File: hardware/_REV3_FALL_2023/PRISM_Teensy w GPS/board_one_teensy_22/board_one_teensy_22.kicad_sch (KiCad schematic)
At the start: 24 parts, among them J1 Micro_SD_Card_Det_Hirose_DM3AT, J3 3387, U1 Teensy4.0, U2 GPS-14414, U3 3966, U4 RFM69HCW_Breakout, U5 SFN-1407PA7.6

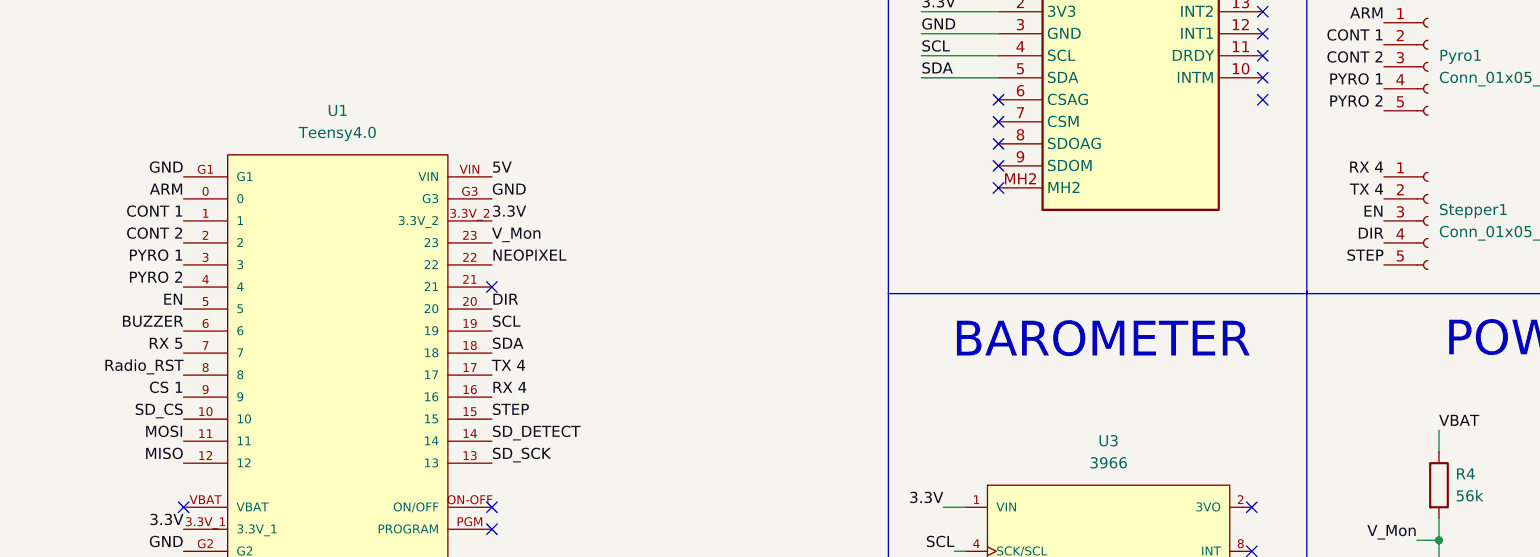
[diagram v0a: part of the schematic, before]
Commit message: fixed stepper wiring
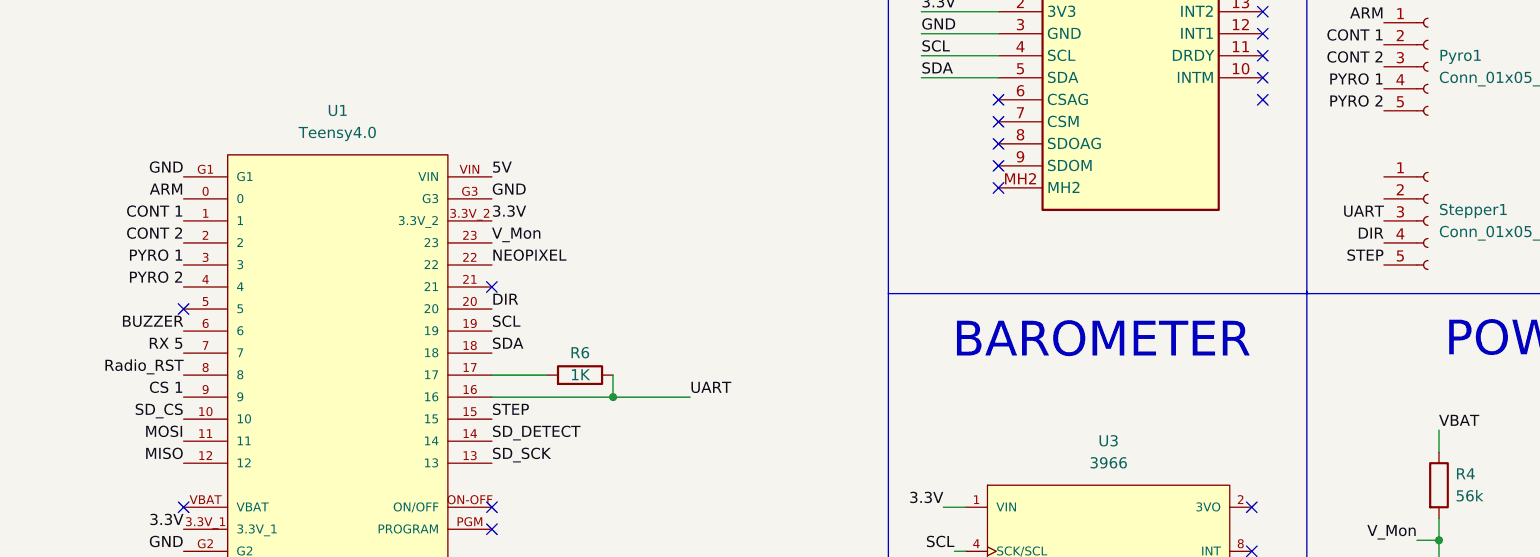
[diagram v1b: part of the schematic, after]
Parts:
- added R6: 1K, Resistor_SMD:R_0603_1608Metric, symbol Device:R
- D3, D5: Vendor (none) -> C2761795
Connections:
- net EN: no longer names the net of U1.5
- net EN: no longer Stepper1.3 (Pin_3)
- net RX 4: no longer names the net of Stepper1.1 (Pin_1)
- net RX 4: no longer U1.16
- net TX 4: no longer names the net of U1.17
- net TX 4: now also R6.2; no longer Stepper1.2 (Pin_2)
- new net UART: R6.1, Stepper1.3 (Pin_3), U1.16
- no-connect marks 35 -> 36
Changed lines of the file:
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@@
   (junction (at 248.92 27.94) (diameter 0) (color 0 0 0 0)
+  )
+  (junction (at 93.98 82.55) (diameter 0) (color 0 0 0 0)
   )
   (junction (at 55.88 177.8) (diameter 0) (color 0 0 0 0)
@@
   (no_connect (at 261.62 97.79))
   (no_connect (at 138.43 35.56))
+  (no_connect (at 44.45 72.39))
   (no_connect (at 261.62 102.87))
   (no_connect (at 138.43 50.8))
@@
     (stroke (width 0) (type default))
   )
+  (wire (pts (xy 93.98 82.55) (xy 102.87 82.55))
+    (stroke (width 0) (type default))
+  )
   (wire (pts (xy 231.14 27.94) (xy 231.14 34.29))
     (stroke (width 0) (type default))
@@
     (stroke (width 0) (type default))
   )
+  (wire (pts (xy 80.01 82.55) (xy 93.98 82.55))
+    (stroke (width 0) (type default))
+  )
   (wire (pts (xy 129.54 45.72) (xy 138.43 45.72))
     (stroke (width 0) (type default))
@@
     (stroke (width 0) (type default))
   )
+  (wire (pts (xy 93.98 80.01) (xy 93.98 82.55))
+    (stroke (width 0) (type default))
+  )
   (wire (pts (xy 40.64 171.45) (xy 34.925 171.45))
     (stroke (width 0) (type default))
@@
   )
   (polyline (pts (xy 125.73 128.905) (xy 173.99 128.905))
+    (stroke (width 0) (type default))
+  )
+  (wire (pts (xy 80.01 80.01) (xy 86.36 80.01))
     (stroke (width 0) (type default))
   )
@@
     (effects (font (size 1.27 1.27)) (justify left bottom))
   )
-  (label "EN" (at 44.45 72.39 180) (fields_autoplaced)
-    (effects (font (size 1.27 1.27)) (justify right bottom))
-  )
   (label "ARM" (at 44.45 59.69 180) (fields_autoplaced)
     (effects (font (size 1.27 1.27)) (justify right bottom))
@@
     (effects (font (size 1.27 1.27)) (justify right bottom))
   )
+  (label "UART" (at 182.88 62.23 180) (fields_autoplaced)
+    (effects (font (size 1.27 1.27)) (justify right bottom))
+  )
   (label "SD_SCK" (at 135.255 171.45 0) (fields_autoplaced)
     (effects (font (size 1.27 1.27)) (justify left bottom))
@@
     (effects (font (size 1.27 1.27)) (justify right bottom))
   )
-  (label "TX 4" (at 182.88 59.69 180) (fields_autoplaced)
-    (effects (font (size 1.27 1.27)) (justify right bottom))
-  )
   (label "SCL" (at 246.38 105.41 180) (fields_autoplaced)
     (effects (font (size 1.27 1.27)) (justify right bottom))
@@
     (effects (font (size 1.27 1.27)) (justify right bottom))
   )
-  (label "RX 4" (at 80.01 82.55 0) (fields_autoplaced)
-    (effects (font (size 1.27 1.27)) (justify left bottom))
-  )
   (label "CONT 2" (at 44.45 64.77 180) (fields_autoplaced)
     (effects (font (size 1.27 1.27)) (justify right bottom))
@@
     (effects (font (size 1.27 1.27)) (justify left bottom))
   )
-  (label "TX 4" (at 80.01 80.01 0) (fields_autoplaced)
-    (effects (font (size 1.27 1.27)) (justify left bottom))
-  )
   (label "MOSI" (at 46.355 172.72 180) (fields_autoplaced)
     (effects (font (size 1.27 1.27)) (justify right bottom))
@@
     (effects (font (size 1.27 1.27)) (justify right bottom))
   )
-  (label "EN" (at 182.88 62.23 180) (fields_autoplaced)
-    (effects (font (size 1.27 1.27)) (justify right bottom))
-  )
   (label "RX 5" (at 44.45 77.47 180) (fields_autoplaced)
     (effects (font (size 1.27 1.27)) (justify right bottom))
@@
     (effects (font (size 1.27 1.27)) (justify right bottom))
   )
-  (label "RX 4" (at 182.88 57.15 180) (fields_autoplaced)
-    (effects (font (size 1.27 1.27)) (justify right bottom))
-  )
   (label "Radio_RST" (at 44.45 80.01 180) (fields_autoplaced)
     (effects (font (size 1.27 1.27)) (justify right bottom))
@@
   (label "CONT 1" (at 182.88 41.91 180) (fields_autoplaced)
     (effects (font (size 1.27 1.27)) (justify right bottom))
+  )
+  (label "UART" (at 102.87 82.55 0) (fields_autoplaced)
+    (effects (font (size 1.27 1.27)) (justify left bottom))
   )
   (label "5V" (at 80.01 57.15 0) (fields_autoplaced)
@@
     (property "Datasheet" "https://cdn-shop.adafruit.com/datasheets/WS2812B.pdf" (at 251.46 45.085 0)
       (effects (font (size 1.27 1.27)) (justify left top) hide)
+    )
+    (property "Vendor" "C2761795" (at 248.92 35.56 0)
+      (effects (font (size 1.27 1.27)) hide)
     )
     (pin "1")
@@
     )
   )
+  (symbol (lib_id "Device:R") (at 90.17 80.01 270) (mirror x) (unit 1)
+    (in_bom yes) (on_board yes) (dnp no)
+    (property "Reference" "R6" (at 90.17 77.47 90)
+      (effects (font (size 1.27 1.27)))
+    )
+    (property "Value" "1K" (at 90.17 80.01 90)
+      (effects (font (size 1.27 1.27)))
+    )
+    (property "Footprint" "Resistor_SMD:R_0603_1608Metric" (at 90.17 81.788 90)
+      (effects (font (size 1.27 1.27)) hide)
+    )
+    (property "Datasheet" "~" (at 90.17 80.01 0)
+      (effects (font (size 1.27 1.27)) hide)
+    )
+    (property "Vendor" "C21190" (at 90.17 80.01 0)
+      (effects (font (size 1.27 1.27)) hide)
+    )
+    (pin "1")
+    (pin "2")
+    (instances
+      (project "board_one_teensy_22"
+        (path "/7a48c3b0-2761-409e-ae2f-7ebae3820225"
+          (reference "R6") (unit 1)
+        )
+      )
+    )
+  )
   (symbol (lib_name "GND_1") (lib_id "power:GND") (at 210.82 106.68 0) (unit 1)
     (in_bom yes) (on_board yes) (dnp no) (fields_autoplaced)
@@
       (effects (font (size 1.27 1.27)) (justify left top) hide)
     )
-    (pin "1")
+    (property "Vendor" "C2761795" (at 267.97 35.56 0)
+      (effects (font (size 1.27 1.27)) hide)
+    )
+    (pin "1")
